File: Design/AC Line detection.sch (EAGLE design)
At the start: 14 parts

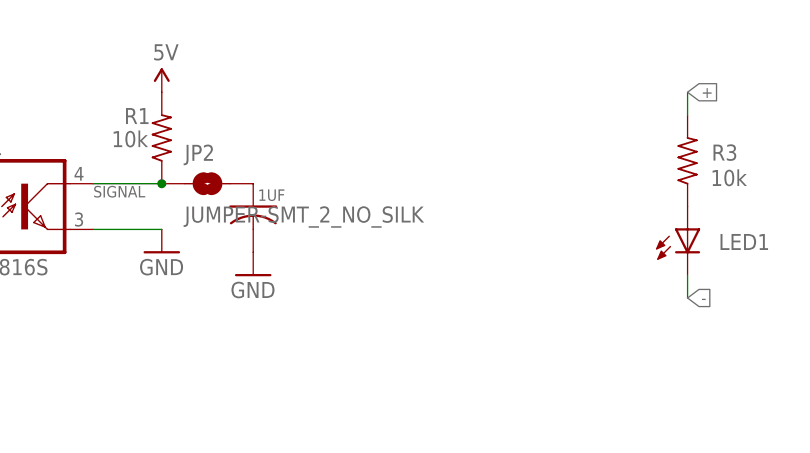
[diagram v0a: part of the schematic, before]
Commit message: Version 1.0
* updated schematics: Added electrolytic capacitor on board
* Updated board: increased dimesnions and new routing
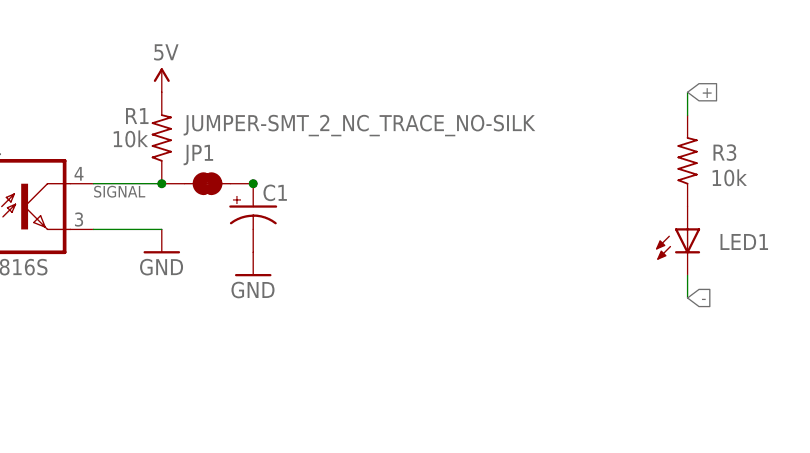
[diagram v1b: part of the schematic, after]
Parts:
- removed 1UF: (no value), edwinRobotics:C-USC0603
- removed JP2: JUMPER-SMT_2_NO_SILK, edwinRobotics:JUMPER-SMT_2_NO_SILK
- added C1: (no value), edwinRobotics:CPOL-US153CLV-0505
- added JP1: JUMPER-SMT_2_NC_TRACE_NO-SILK, edwinRobotics:JUMPER-SMT_2_NC_TRACE_NO-SILK
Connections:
- net GND: now also C1.-; no longer 1UF.2
- net N$2: now also C1.+, JP1.2; no longer 1UF.1, JP2.2
- net SIGNAL: now also JP1.1; no longer JP2.1
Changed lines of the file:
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@@
 <part name="U$4" library="edwinRobotics" deviceset="5V" device=""/>
 <part name="GND3" library="edwinRobotics" deviceset="GND" device=""/>
-<part name="1UF" library="edwinRobotics" deviceset="C-US" device="C0603"/>
 <part name="R3" library="edwinRobotics" deviceset="R-US_" device="R1206" value="10k"/>
 <part name="LED1" library="edwinRobotics" deviceset="LED_TH/SMD" device="CHIPLED_0603"/>
-<part name="JP2" library="edwinRobotics" deviceset="JUMPER-SMT_2_NO" device="_SILK"/>
+<part name="JP1" library="edwinRobotics" deviceset="JUMPER-SMT_2_NC_TRACE" device="_NO-SILK"/>
+<part name="C1" library="edwinRobotics" deviceset="CPOL-US" device="153CLV-0505"/>
 </parts>
 <sheets>
@@
 <attribute name="VALUE" x="193.04" y="96.52" size="1.778" layer="96"/>
 </instance>
-<instance part="1UF" gate="G$1" x="195.58" y="106.68" smashed="yes">
-<attribute name="NAME" x="196.088" y="107.315" size="1.27" layer="95" font="vector" ratio="10"/>
-<attribute name="VALUE" x="196.596" y="102.489" size="1.778" layer="96"/>
-</instance>
 <instance part="R3" gate="G$1" x="243.84" y="111.76" smashed="yes" rot="R90">
 <attribute name="NAME" x="249.428" y="113.5634" size="1.778" layer="95" rot="R180"/>
@@
 <attribute name="VALUE" x="249.555" y="99.568" size="1.778" layer="96" rot="R90"/>
 </instance>
-<instance part="JP2" gate="G$1" x="190.5" y="109.22"/>
+<instance part="JP1" gate="G$1" x="190.5" y="109.22" smashed="yes">
+<attribute name="NAME" x="187.96" y="111.76" size="1.778" layer="95" font="vector"/>
+<attribute name="VALUE" x="187.96" y="116.84" size="1.778" layer="96" font="vector" align="top-left"/>
+</instance>
+<instance part="C1" gate="G$1" x="195.58" y="106.68"/>
 </instances>
 <busses>
@@
 <wire x1="177.8" y1="109.22" x2="185.42" y2="109.22" width="0.1524" layer="91"/>
 <label x="177.8" y="107.696" size="1.27" layer="95" font="vector" ratio="10"/>
-<pinref part="JP2" gate="G$1" pin="1"/>
 <junction x="185.42" y="109.22"/>
+<pinref part="JP1" gate="G$1" pin="1"/>
 </segment>
 </net>
@@
 <segment>
 <pinref part="GND3" gate="1" pin="GND"/>
-<pinref part="1UF" gate="G$1" pin="2"/>
+<pinref part="C1" gate="G$1" pin="-"/>
 </segment>
 </net>
@@
 <net name="N$2" class="0">
 <segment>
-<pinref part="1UF" gate="G$1" pin="1"/>
-<pinref part="JP2" gate="G$1" pin="2"/>
+<pinref part="JP1" gate="G$1" pin="2"/>
+<junction x="195.58" y="109.22"/>
+<pinref part="JP1" gate="G$1" pin="2"/>
+<pinref part="C1" gate="G$1" pin="+"/>
 </segment>
 </net>

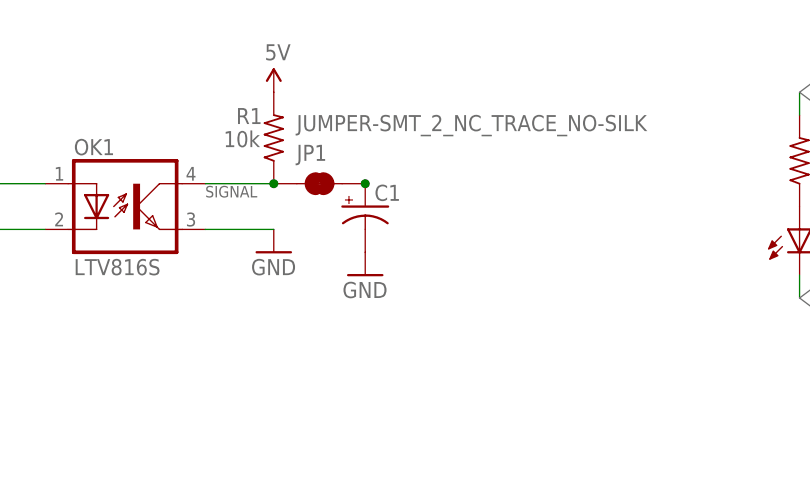
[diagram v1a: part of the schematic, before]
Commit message: version 1.0 update:
* Updated Capacitor Pad Size
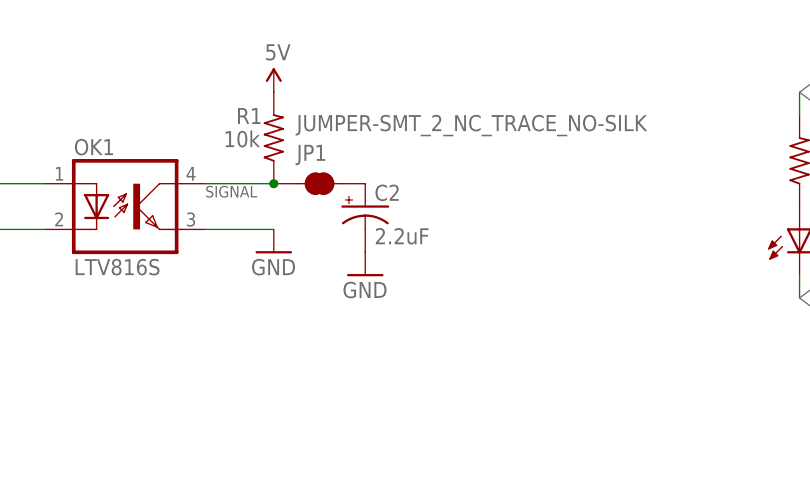
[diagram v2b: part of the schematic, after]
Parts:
- removed C1: (no value), edwinRobotics:CPOL-US153CLV-0505
- added C2: 2.2uF, edwinRobotics:CPOL-USCAP-4X5MM
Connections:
- net GND: now also C2.-; no longer C1.-
- net N$2: now also C2.+; no longer C1.+
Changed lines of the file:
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@@
 <part name="LED1" library="edwinRobotics" deviceset="LED_TH/SMD" device="CHIPLED_0603"/>
 <part name="JP1" library="edwinRobotics" deviceset="JUMPER-SMT_2_NC_TRACE" device="_NO-SILK"/>
-<part name="C1" library="edwinRobotics" deviceset="CPOL-US" device="153CLV-0505"/>
+<part name="C2" library="edwinRobotics" deviceset="CPOL-US" device="CAP-4X5MM" value="2.2uF"/>
 </parts>
 <sheets>
@@
 <attribute name="VALUE" x="187.96" y="116.84" size="1.778" layer="96" font="vector" align="top-left"/>
 </instance>
-<instance part="C1" gate="G$1" x="195.58" y="106.68"/>
+<instance part="C2" gate="G$1" x="195.58" y="106.68"/>
 </instances>
 <busses>
@@
 <segment>
 <pinref part="GND3" gate="1" pin="GND"/>
-<pinref part="C1" gate="G$1" pin="-"/>
+<pinref part="C2" gate="G$1" pin="-"/>
 </segment>
 </net>
@@
 <segment>
 <pinref part="JP1" gate="G$1" pin="2"/>
-<junction x="195.58" y="109.22"/>
-<pinref part="JP1" gate="G$1" pin="2"/>
-<pinref part="C1" gate="G$1" pin="+"/>
+<pinref part="C2" gate="G$1" pin="+"/>
 </segment>
 </net>

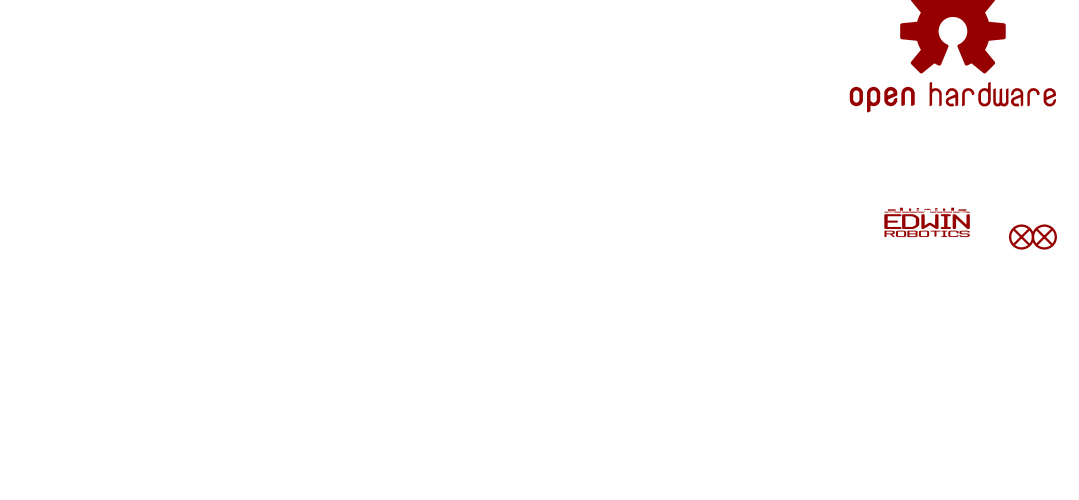
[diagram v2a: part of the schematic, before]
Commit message: *Removed production files* *Added Licesence and readme file*
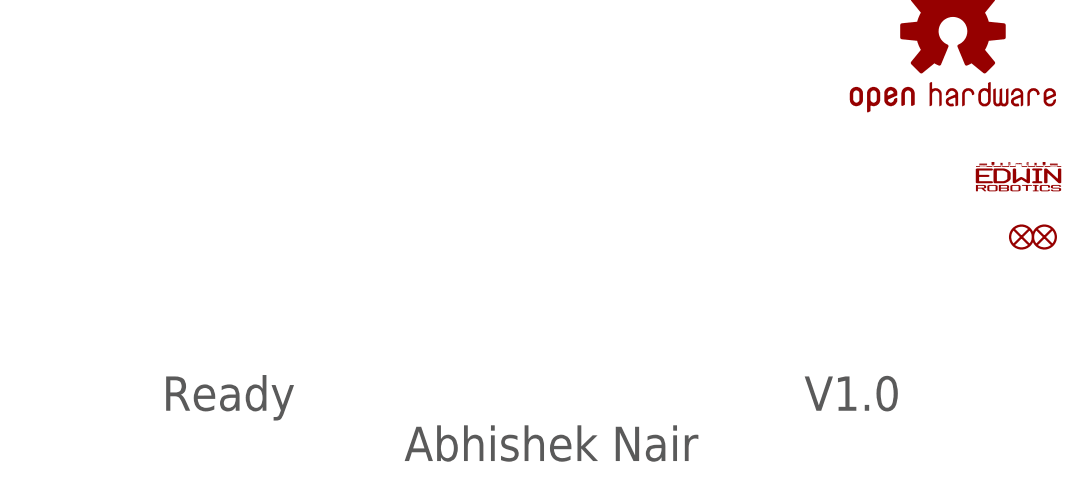
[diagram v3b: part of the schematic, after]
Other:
- note added: "Abhishek Nair"
- note added: "Ready"
- note added: "V1.0"
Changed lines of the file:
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@@
 <sheet>
 <plain>
+<text x="171.196" y="6.096" size="3.81" layer="97">Ready</text>
+<text x="242.57" y="6.096" size="3.81" layer="97">V1.0</text>
+<text x="198.12" y="0.508" size="3.81" layer="97">Abhishek Nair</text>
 </plain>
 <instances>
@@
 <instance part="FID1" gate="G$1" x="269.24" y="25.4"/>
 <instance part="FID2" gate="G$1" x="266.7" y="25.4"/>
-<instance part="U$1" gate="G$1" x="251.46" y="25.4"/>
+<instance part="U$1" gate="G$1" x="261.62" y="30.48"/>
 <instance part="LOGO1" gate="G$1" x="259.08" y="48.26"/>
 <instance part="B1" gate="G$1" x="104.14" y="109.22" smashed="yes">

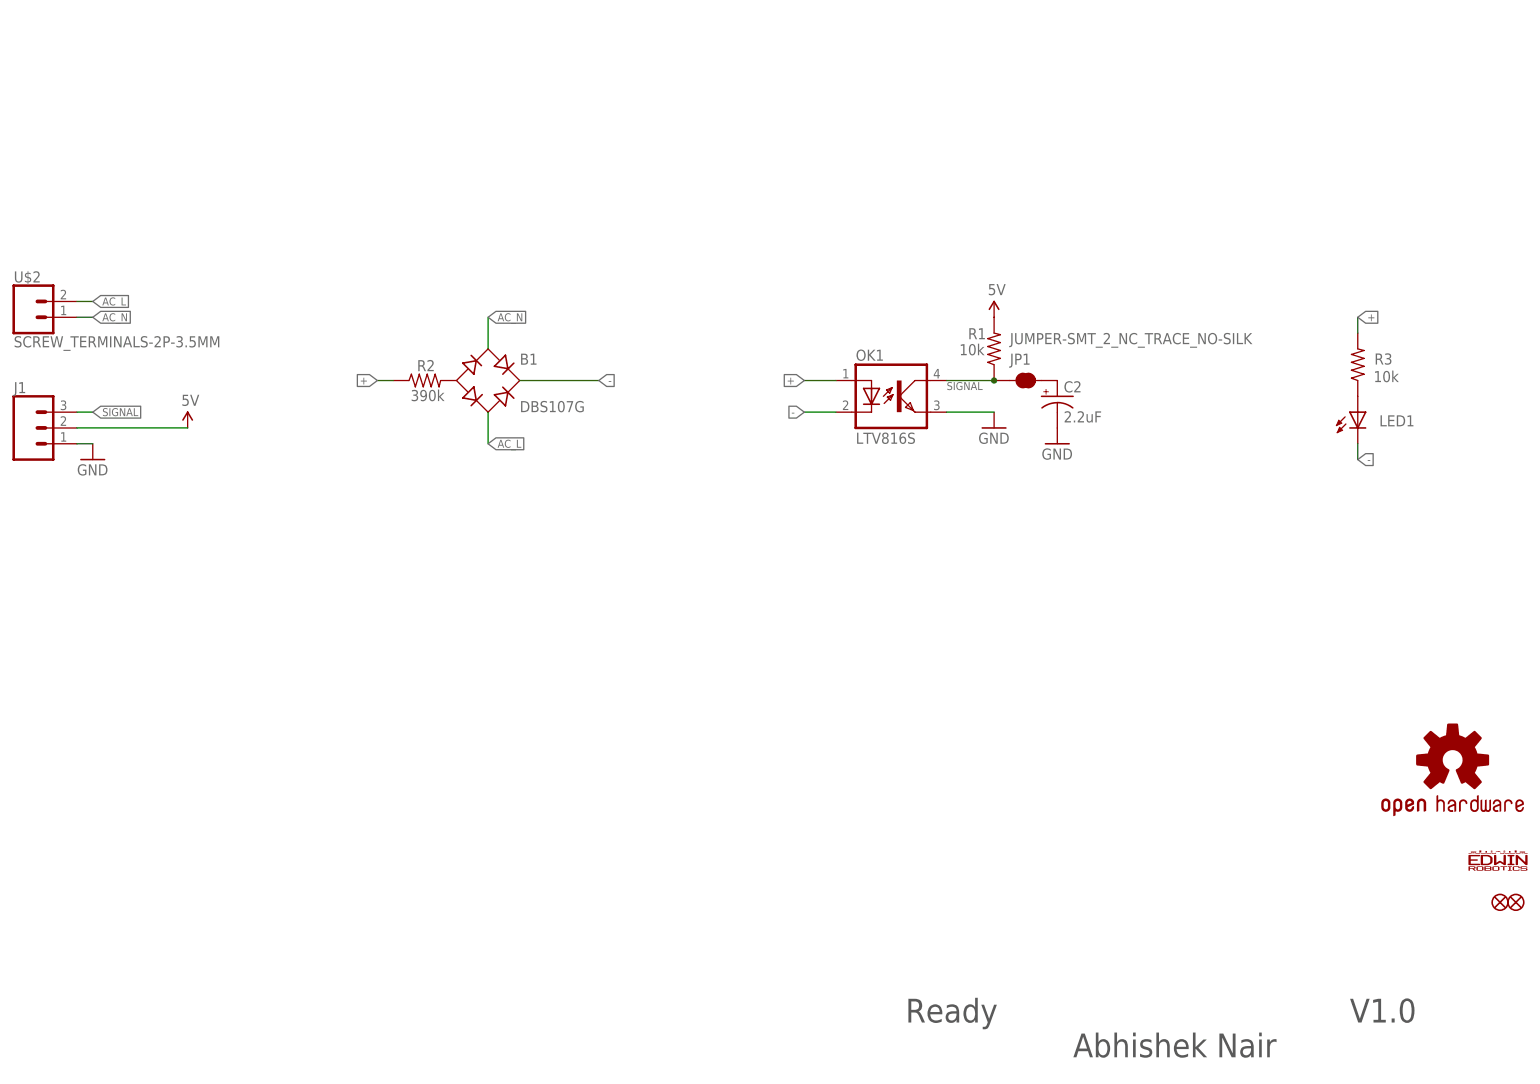
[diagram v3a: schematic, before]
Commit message: Version 2.0:
Major Changes:
*Updated Design FIles
* Updated the board Size
* Added mounting Holes
* Added Debug LED and enable/Disbale Jumper
* Replaced Screw terminal with KF126
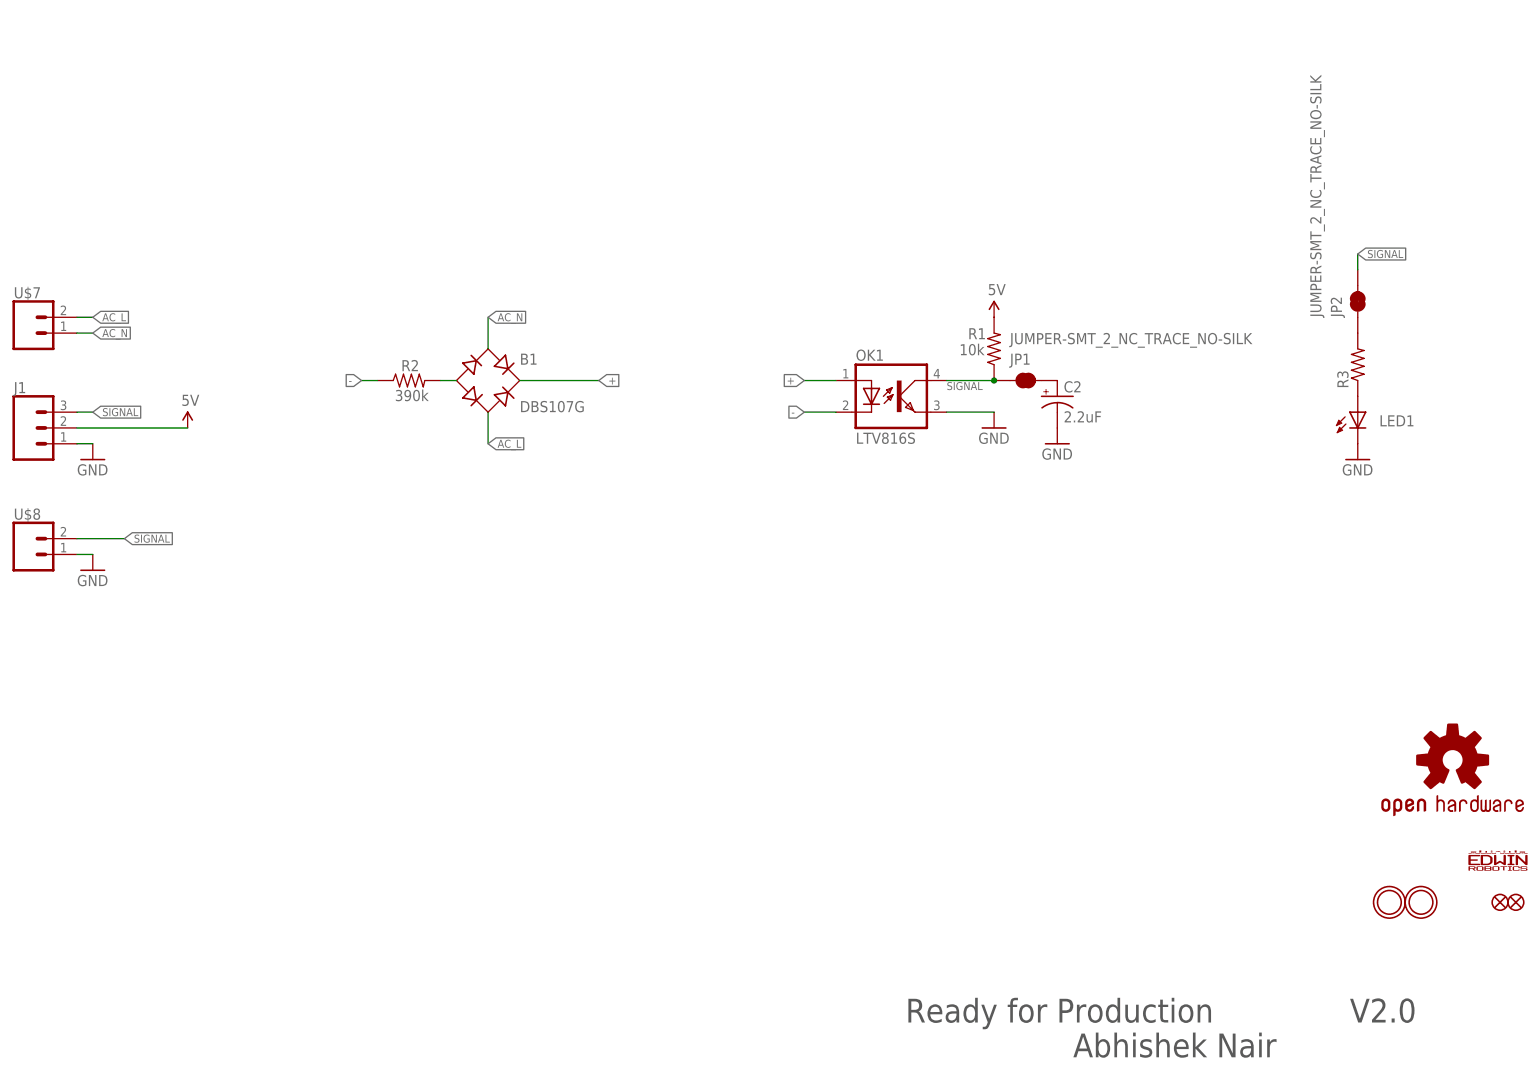
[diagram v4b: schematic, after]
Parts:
- removed U$2: SCREW_TERMINALS-2P-3.5MM, edwinRobotics:SCREW_TERMINALS-2P-3.5MM
- added JP2: JUMPER-SMT_2_NC_TRACE_NO-SILK, edwinRobotics:JUMPER-SMT_2_NC_TRACE_NO-SILK
- added U$5, U$6: MOUNTINGHOLE3.0THIN, edwinRobotics:MOUNTINGHOLE3.0THIN
- added U$7, U$8: SCREW_TERMINALS-2P-5MM, edwinRobotics:SCREW_TERMINALS-2P-5MM
- R3: value 10k -> (none); device edwinRobotics:R-US_R1206 -> edwinRobotics:R-US_R0603
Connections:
- new net N$4: JP2.1, R3.2
- net +: now also B1.+; no longer R2.1, R3.2
- net -: now also R2.1; no longer B1.+, LED1.C
- net AC_L: now also U$7.2; no longer U$2.2
- net AC_N: now also U$7.1; no longer U$2.1
- net GND: now also LED1.C, U$8.1
- net SIGNAL: now also JP2.2, U$8.2
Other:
- note added: "Ready for Production"
- note added: "V2.0"
- note removed: "Ready"
- note removed: "V1.0"
- moved on the sheet: R2

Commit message: Version 2.0: Added Gerber Files
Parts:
- R3: value (none) -> 100R/330R
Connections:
- net 5V: now also LED1.A
- net GND: no longer LED1.C
- net N$3: now also LED1.C; no longer LED1.A
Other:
- moved on the sheet: JP2, LED1, R3
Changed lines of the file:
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@@
 <?xml version="1.0" encoding="utf-8"?>
 <!DOCTYPE eagle SYSTEM "eagle.dtd">
-<eagle version="8.7.1">
+<eagle version="9.0.0">
 <drawing>
 <settings>
@@
 <part name="C2" library="edwinRobotics" deviceset="CPOL-US" device="CAP-4X5MM" value="2.2uF"/>
 <part name="JP2" library="edwinRobotics" deviceset="JUMPER-SMT_2_NC_TRACE" device="_NO-SILK"/>
-<part name="GND4" library="edwinRobotics" deviceset="GND" device=""/>
-<part name="R3" library="edwinRobotics" deviceset="R-US_" device="R0603"/>
+<part name="R3" library="edwinRobotics" deviceset="R-US_" device="R0603" value="100R/330R"/>
 <part name="U$5" library="edwinRobotics" deviceset="MOUNTINGHOLE" device="3.0THIN"/>
 <part name="U$6" library="edwinRobotics" deviceset="MOUNTINGHOLE" device="3.0THIN"/>
@@
 <part name="U$8" library="edwinRobotics" deviceset="SCREW_TERMINALS-2P-" device="5MM"/>
 <part name="U$7" library="edwinRobotics" deviceset="SCREW_TERMINALS-2P-" device="5MM"/>
+<part name="U$2" library="edwinRobotics" deviceset="5V" device=""/>
 </parts>
 <sheets>
@@
 <attribute name="VALUE" x="193.04" y="96.52" size="1.778" layer="96"/>
 </instance>
-<instance part="LED1" gate="G$1" x="243.84" y="104.14" smashed="yes">
-<attribute name="NAME" x="252.984" y="103.632" size="1.778" layer="95" rot="R180"/>
-<attribute name="VALUE" x="249.555" y="99.568" size="1.778" layer="96" rot="R90"/>
+<instance part="LED1" gate="G$1" x="254" y="116.84" smashed="yes">
+<attribute name="NAME" x="256.286" y="119.634" size="1.778" layer="95" rot="R270"/>
+<attribute name="VALUE" x="259.715" y="112.268" size="1.778" layer="96" rot="R90"/>
 </instance>
 <instance part="JP1" gate="G$1" x="190.5" y="109.22" smashed="yes">
@@
 </instance>
 <instance part="C2" gate="G$1" x="195.58" y="106.68"/>
-<instance part="JP2" gate="G$1" x="243.84" y="121.92" smashed="yes" rot="R90">
-<attribute name="NAME" x="241.3" y="119.38" size="1.778" layer="95" font="vector" rot="R90"/>
-<attribute name="VALUE" x="236.22" y="119.38" size="1.778" layer="96" font="vector" rot="R90" align="top-left"/>
-</instance>
-<instance part="GND4" gate="1" x="243.84" y="96.52" smashed="yes">
-<attribute name="VALUE" x="241.3" y="93.98" size="1.778" layer="96"/>
-</instance>
-<instance part="R3" gate="G$1" x="243.84" y="111.76" rot="R90"/>
+<instance part="JP2" gate="G$1" x="254" y="96.52" smashed="yes" rot="R270">
+<attribute name="NAME" x="256.54" y="99.06" size="1.778" layer="95" font="vector" rot="R270"/>
+<attribute name="VALUE" x="262.636" y="127.254" size="1.778" layer="96" font="vector" rot="R270" align="top-left"/>
+</instance>
+<instance part="R3" gate="G$1" x="254" y="106.68" smashed="yes" rot="R270">
+<attribute name="NAME" x="255.524" y="105.8926" size="1.778" layer="95"/>
+<attribute name="VALUE" x="237.236" y="105.664" size="1.778" layer="96"/>
+</instance>
 <instance part="U$5" gate="G$1" x="248.92" y="25.4"/>
 <instance part="U$6" gate="G$1" x="254" y="25.4"/>
@@
 <instance part="U$7" gate="G$1" x="30.48" y="116.84" smashed="yes">
 <attribute name="NAME" x="27.94" y="122.428" size="1.778" layer="95" font="vector"/>
+</instance>
+<instance part="U$2" gate="G$1" x="254" y="119.38" smashed="yes">
+<attribute name="VALUE" x="252.984" y="122.936" size="1.778" layer="96"/>
 </instance>
 </instances>
@@
 <segment>
 <pinref part="JP2" gate="G$1" pin="2"/>
-<wire x1="243.84" y1="127" x2="243.84" y2="129.54" width="0.1524" layer="91"/>
-<label x="243.84" y="129.54" size="1.27" layer="95" xref="yes"/>
+<wire x1="254" y1="91.44" x2="251.46" y2="91.44" width="0.1524" layer="91"/>
+<label x="251.46" y="91.44" size="1.27" layer="95" rot="R180" xref="yes"/>
 </segment>
 <segment>
@@
 </segment>
 <segment>
-<pinref part="LED1" gate="G$1" pin="C"/>
-<pinref part="GND4" gate="1" pin="GND"/>
-</segment>
-<segment>
 <pinref part="GND5" gate="1" pin="GND"/>
 <pinref part="U$8" gate="G$1" pin="1"/>
@@
 <pinref part="U$4" gate="G$1" pin="5V"/>
 </segment>
+<segment>
+<pinref part="U$2" gate="G$1" pin="5V"/>
+<pinref part="LED1" gate="G$1" pin="A"/>
+</segment>
 </net>
 <net name="N$2" class="0">
@@
 </segment>
 </net>
-<net name="N$3" class="0">
-<segment>
-<pinref part="LED1" gate="G$1" pin="A"/>
-<pinref part="R3" gate="G$1" pin="1"/>
-</segment>
-</net>
 <net name="N$4" class="0">
 <segment>
@@
 </segment>
 </net>
+<net name="N$3" class="0">
+<segment>
+<pinref part="R3" gate="G$1" pin="1"/>
+<pinref part="LED1" gate="G$1" pin="C"/>
+</segment>
+</net>
